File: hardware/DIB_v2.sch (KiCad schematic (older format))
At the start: 1 part, among them J3 28-pin module socket

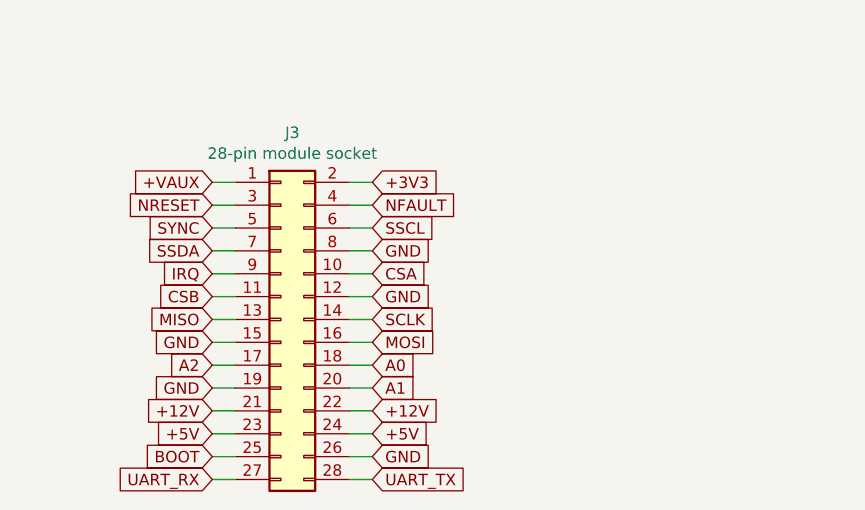
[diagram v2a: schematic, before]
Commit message: Adding ULX3S connections
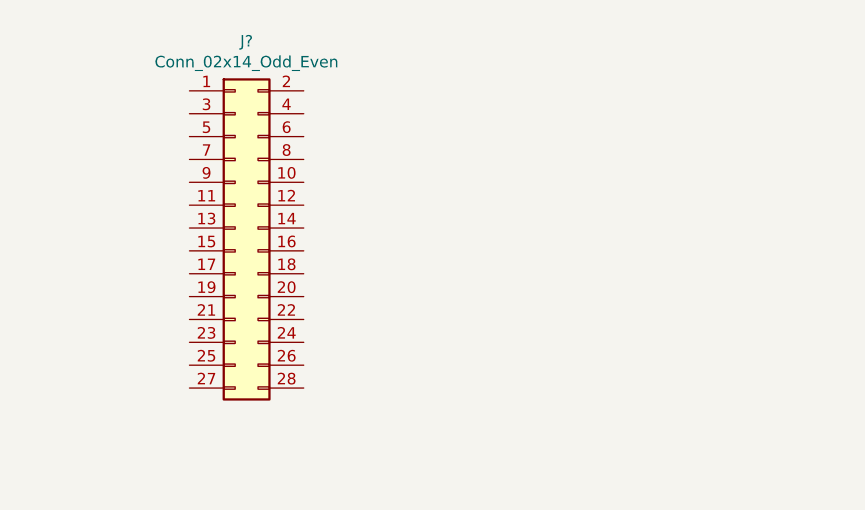
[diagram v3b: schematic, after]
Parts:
- removed J3: 28-pin module socket, Connector_PinHeader_2.54mm:PinHeader_2x14_P2.54mm_Horizontal, symbol Connector_Generic:Conn_02x14_Odd_Even
- added J?: Conn_02x14_Odd_Even, Connector_PinHeader_2.54mm:PinHeader_2x14_P2.54mm_Horizontal, symbol Connector_Generic:Conn_02x14_Odd_Even
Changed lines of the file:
@@
 $EndDescr
 $Comp
-L Connector_Generic:Conn_02x14_Odd_Even J3
-U 1 1 5E22D098
-P 1700 2150
-F 0 "J3" H 1750 2967 50  0000 C CNN
-F 1 "28-pin module socket" H 1750 2876 50  0000 C CNN
-F 2 "Connector_PinHeader_2.54mm:PinHeader_2x14_P2.54mm_Horizontal" H 1700 2150 50  0001 C CNN
-F 3 "~" H 1700 2150 50  0001 C CNN
-	1    1700 2150
+L Connector_Generic:Conn_02x14_Odd_Even J?
+U 1 1 5E5C1881
+P 1500 1750
+AR Path="/5E5C1881" Ref="J?"  Part="1"
+AR Path="/5E22C9F9/5E5C1881" Ref="J?"  Part="1"
+AR Path="/5E22D00E/5E5C1881" Ref="J?"  Part="1"
+F 0 "J?" H 1550 2567 50  0000 C CNN
+F 1 "Conn_02x14_Odd_Even" H 1550 2476 50  0000 C CNN
+F 2 "Connector_PinHeader_2.54mm:PinHeader_2x14_P2.54mm_Horizontal" H 1500 1750 50  0001 C CNN
+F 3 "~" H 1500 1750 50  0001 C CNN
+	1    1500 1750
 	1    0    0    -1
 $EndComp
-Text GLabel 1400 1550 0    50   Input ~ 0
-+VAUX
-Text GLabel 1400 1650 0    50   Input ~ 0
-NRESET
-Text GLabel 1400 1750 0    50   Input ~ 0
-SYNC
-Text GLabel 1400 1850 0    50   Input ~ 0
-SSDA
-Text GLabel 1400 1950 0    50   Input ~ 0
-IRQ
-Text GLabel 1400 2050 0    50   Input ~ 0
-CSB
-Text GLabel 1400 2150 0    50   Input ~ 0
-MISO
-Text GLabel 1400 2250 0    50   Input ~ 0
-GND
-Text GLabel 1400 2350 0    50   Input ~ 0
-A2
-Text GLabel 1400 2450 0    50   Input ~ 0
-GND
-Text GLabel 1400 2550 0    50   Input ~ 0
-+12V
-Text GLabel 1400 2650 0    50   Input ~ 0
-+5V
-Text GLabel 1400 2750 0    50   Input ~ 0
-BOOT
-Text GLabel 1400 2850 0    50   Input ~ 0
-UART_RX
-Text GLabel 2100 1550 2    50   Input ~ 0
-+3V3
-Text GLabel 2100 1650 2    50   Input ~ 0
-NFAULT
-Text GLabel 2100 1750 2    50   Input ~ 0
-SSCL
-Text GLabel 2100 1850 2    50   Input ~ 0
-GND
-Text GLabel 2100 2050 2    50   Input ~ 0
-GND
-Text GLabel 2100 1950 2    50   Input ~ 0
-CSA
-Text GLabel 2100 2150 2    50   Input ~ 0
-SCLK
-Text GLabel 2100 2250 2    50   Input ~ 0
-MOSI
-Text GLabel 2100 2350 2    50   Input ~ 0
-A0
-Text GLabel 2100 2450 2    50   Input ~ 0
-A1
-Text GLabel 2100 2550 2    50   Input ~ 0
-+12V
-Text GLabel 2100 2650 2    50   Input ~ 0
-+5V
-Text GLabel 2100 2750 2    50   Input ~ 0
-GND
-Text GLabel 2100 2850 2    50   Input ~ 0
-UART_TX
-Wire Wire Line
-	1400 1550 1500 1550
-Wire Wire Line
-	1400 1650 1500 1650
-Wire Wire Line
-	2000 1550 2100 1550
-Wire Wire Line
-	2000 1650 2100 1650
-Wire Wire Line
-	1400 1750 1500 1750
-Wire Wire Line
-	2000 1750 2100 1750
-Wire Wire Line
-	1400 1850 1500 1850
-Wire Wire Line
-	2000 1850 2100 1850
-Wire Wire Line
-	1400 1950 1500 1950
-Wire Wire Line
-	2000 1950 2100 1950
-Wire Wire Line
-	2100 2050 2000 2050
-Wire Wire Line
-	1400 2050 1500 2050
-Wire Wire Line
-	1400 2150 1500 2150
-Wire Wire Line
-	2000 2150 2100 2150
-Wire Wire Line
-	2100 2250 2000 2250
-Wire Wire Line
-	1400 2250 1500 2250
-Wire Wire Line
-	1400 2350 1500 2350
-Wire Wire Line
-	1400 2450 1500 2450
-Wire Wire Line
-	1500 2550 1400 2550
-Wire Wire Line
-	1400 2650 1500 2650
-Wire Wire Line
-	1400 2750 1500 2750
-Wire Wire Line
-	1400 2850 1500 2850
-Wire Wire Line
-	2000 2850 2100 2850
-Wire Wire Line
-	2100 2750 2000 2750
-Wire Wire Line
-	2000 2650 2100 2650
-Wire Wire Line
-	2100 2550 2000 2550
-Wire Wire Line
-	2000 2450 2100 2450
-Wire Wire Line
-	2100 2350 2000 2350
 $EndSCHEMATC

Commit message: Assigning footprints
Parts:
- removed J?: Conn_02x14_Odd_Even, Connector_PinHeader_2.54mm:PinHeader_2x14_P2.54mm_Horizontal, symbol Connector_Generic:Conn_02x14_Odd_Even
- added J6: Conn_02x10_Odd_Even, Connector_PinHeader_2.54mm:PinHeader_2x10_P2.54mm_Horizontal, symbol Connector_Generic:Conn_02x10_Odd_Even
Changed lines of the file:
@@
 $EndDescr
 $Comp
-L Connector_Generic:Conn_02x14_Odd_Even J?
-U 1 1 5E5C1881
-P 1500 1750
-AR Path="/5E5C1881" Ref="J?"  Part="1"
-AR Path="/5E22C9F9/5E5C1881" Ref="J?"  Part="1"
-AR Path="/5E22D00E/5E5C1881" Ref="J?"  Part="1"
-F 0 "J?" H 1550 2567 50  0000 C CNN
-F 1 "Conn_02x14_Odd_Even" H 1550 2476 50  0000 C CNN
-F 2 "Connector_PinHeader_2.54mm:PinHeader_2x14_P2.54mm_Horizontal" H 1500 1750 50  0001 C CNN
-F 3 "~" H 1500 1750 50  0001 C CNN
-	1    1500 1750
+L Connector_Generic:Conn_02x10_Odd_Even J6
+U 1 1 5E2F30CC
+P 3650 1500
+F 0 "J6" H 3700 2117 50  0000 C CNN
+F 1 "Conn_02x10_Odd_Even" H 3700 2026 50  0000 C CNN
+F 2 "Connector_PinHeader_2.54mm:PinHeader_2x10_P2.54mm_Horizontal" H 3650 1500 50  0001 C CNN
+F 3 "~" H 3650 1500 50  0001 C CNN
+	1    3650 1500
 	1    0    0    -1
 $EndComp

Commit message: Adding last known changes to shematics
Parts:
- removed J6: Conn_02x10_Odd_Even, Connector_PinHeader_2.54mm:PinHeader_2x10_P2.54mm_Horizontal, symbol Connector_Generic:Conn_02x10_Odd_Even
- added J?: DIB_V2, Connector_PinHeader_2.54mm:PinHeader_2x10_P2.54mm_Horizontal, symbol Connector_Generic:Conn_02x10_Odd_Even
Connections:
- new net 14N: J?.8 (Pin_8)
- new net 14P: J?.7 (Pin_7)
- new net 15N: J?.6 (Pin_6)
- new net 15P: J?.5 (Pin_5)
- new net 16N: J?.4 (Pin_4)
- new net 16P: J?.3 (Pin_3)
- new net 17N: J?.2 (Pin_2)
- new net 17P: J?.1 (Pin_1)
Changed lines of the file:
@@
 $Descr A4 11693 8268
 encoding utf-8
-Sheet 5 11
+Sheet 5 10
 Title ""
-Date ""
-Rev ""
-Comp ""
+Date "2020-01-29"
+Rev "0.1"
+Comp "Envox d.o.o."
 Comment1 ""
 Comment2 ""
@@
 Comment4 ""
 $EndDescr
+Text GLabel 1950 2350 0    50   Input ~ 0
+FPGA_CLK_OUT
+Text GLabel 2150 2350 2    50   Input ~ 0
+17P
+Wire Wire Line
+	2150 2350 1950 2350
 $Comp
-L Connector_Generic:Conn_02x10_Odd_Even J6
-U 1 1 5E2F30CC
-P 3650 1500
-F 0 "J6" H 3700 2117 50  0000 C CNN
-F 1 "Conn_02x10_Odd_Even" H 3700 2026 50  0000 C CNN
-F 2 "Connector_PinHeader_2.54mm:PinHeader_2x10_P2.54mm_Horizontal" H 3650 1500 50  0001 C CNN
-F 3 "~" H 3650 1500 50  0001 C CNN
-	1    3650 1500
+L Connector_Generic:Conn_02x10_Odd_Even J?
+U 1 1 5E84CF5B
+P 1800 1600
+AR Path="/5E22D00E/5E84CF5B" Ref="J?"  Part="1"
+AR Path="/5E22C01C/5E84CF5B" Ref="J?"  Part="1"
+F 0 "J?" H 1850 2217 50  0000 C CNN
+F 1 "DIB_V2" H 1850 2126 50  0000 C CNN
+F 2 "Connector_PinHeader_2.54mm:PinHeader_2x10_P2.54mm_Horizontal" H 1800 1600 50  0001 C CNN
+F 3 "~" H 1800 1600 50  0001 C CNN
+	1    1800 1600
 	1    0    0    -1
 $EndComp
+Text GLabel 1500 1200 0    50   Input ~ 0
+17P
+Text GLabel 1500 1300 0    50   Input ~ 0
+16P
+Text GLabel 1500 1400 0    50   Input ~ 0
+15P
+Text GLabel 1500 1500 0    50   Input ~ 0
+14P
+Text GLabel 2200 1200 2    50   Input ~ 0
+17N
+Text GLabel 2200 1300 2    50   Input ~ 0
+16N
+Text GLabel 2200 1400 2    50   Input ~ 0
+15N
+Text GLabel 2200 1500 2    50   Input ~ 0
+14N
+Wire Wire Line
+	1500 1200 1600 1200
+Wire Wire Line
+	1500 1300 1600 1300
+Wire Wire Line
+	1500 1400 1600 1400
+Wire Wire Line
+	1500 1500 1600 1500
+Wire Wire Line
+	2100 1200 2200 1200
+Wire Wire Line
+	2100 1300 2200 1300
+Wire Wire Line
+	2100 1400 2200 1400
+Wire Wire Line
+	2100 1500 2200 1500
 $EndSCHEMATC

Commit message: Renaming wires
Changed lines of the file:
@@
 $EndDescr
 Text GLabel 1950 2350 0    50   Input ~ 0
-FPGA_CLK_OUT
+DIB2_FPGA_CLK_OUT
 Text GLabel 2150 2350 2    50   Input ~ 0
 17P

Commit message: Routing board
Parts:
- gave numbers to parts that had none: 1
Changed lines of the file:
@@
 	2150 2350 1950 2350
 $Comp
-L Connector_Generic:Conn_02x10_Odd_Even J?
+L Connector_Generic:Conn_02x10_Odd_Even J9
 U 1 1 5E84CF5B
 P 1800 1600
-AR Path="/5E22D00E/5E84CF5B" Ref="J?"  Part="1"
+AR Path="/5E22D00E/5E84CF5B" Ref="J9"  Part="1"
 AR Path="/5E22C01C/5E84CF5B" Ref="J?"  Part="1"
-F 0 "J?" H 1850 2217 50  0000 C CNN
+F 0 "J9" H 1850 2217 50  0000 C CNN
 F 1 "DIB_V2" H 1850 2126 50  0000 C CNN
 F 2 "Connector_PinHeader_2.54mm:PinHeader_2x10_P2.54mm_Horizontal" H 1800 1600 50  0001 C CNN

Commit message: Before AGND - GND
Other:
- note added: "DIB2_FPGA_CLK_OUT"
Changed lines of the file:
@@
 Comment4 ""
 $EndDescr
-Text GLabel 1950 2350 0    50   Input ~ 0
-DIB2_FPGA_CLK_OUT
-Text GLabel 2150 2350 2    50   Input ~ 0
-17P
-Wire Wire Line
-	2150 2350 1950 2350
 $Comp
 L Connector_Generic:Conn_02x10_Odd_Even J9
@@
 Wire Wire Line
 	2100 1500 2200 1500
+Text Notes 550  1250 0    50   ~ 0
+DIB2_FPGA_CLK_OUT
 $EndSCHEMATC
